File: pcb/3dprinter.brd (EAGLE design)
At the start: 100 x 80 mm, 24 parts, among them IC1 NRF51822, IC2 TMC2100

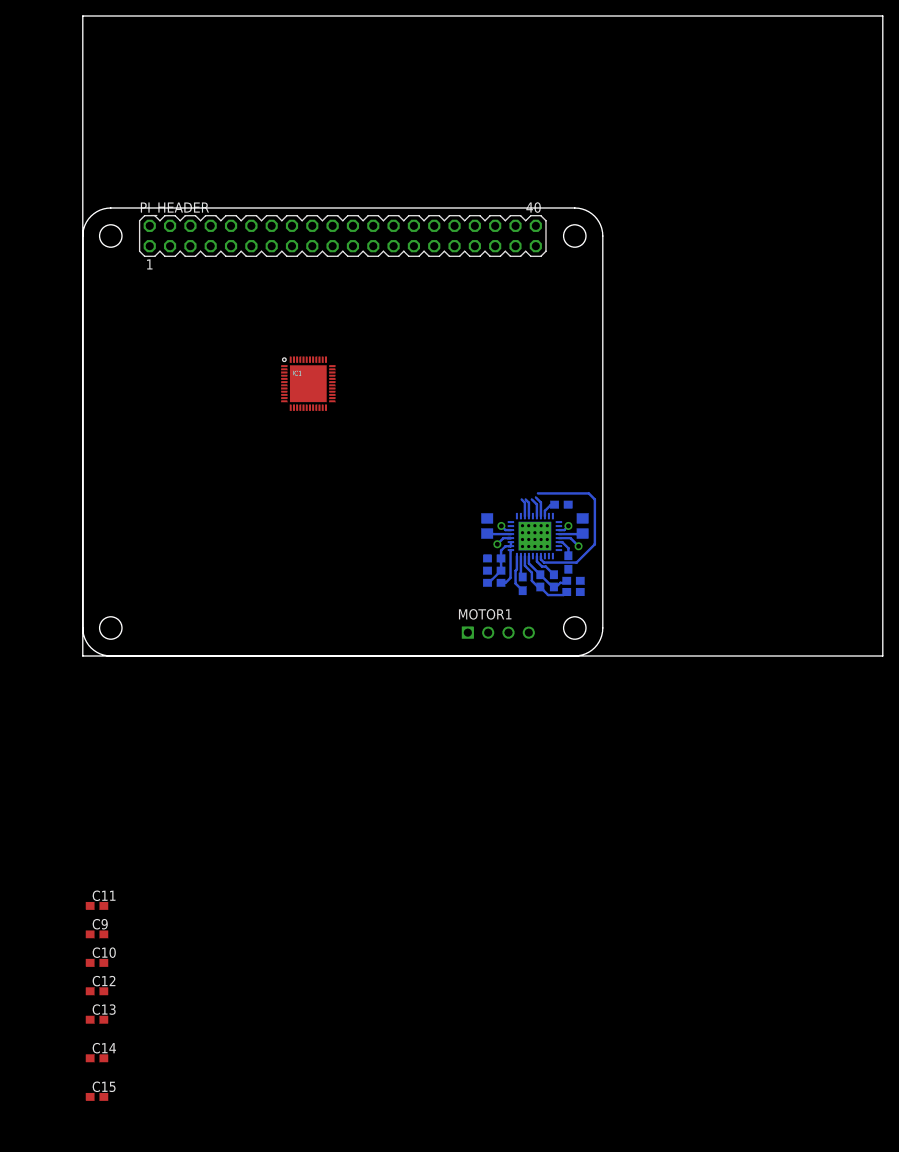
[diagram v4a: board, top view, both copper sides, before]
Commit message: Multiplied motor driver circuit and added mosfets
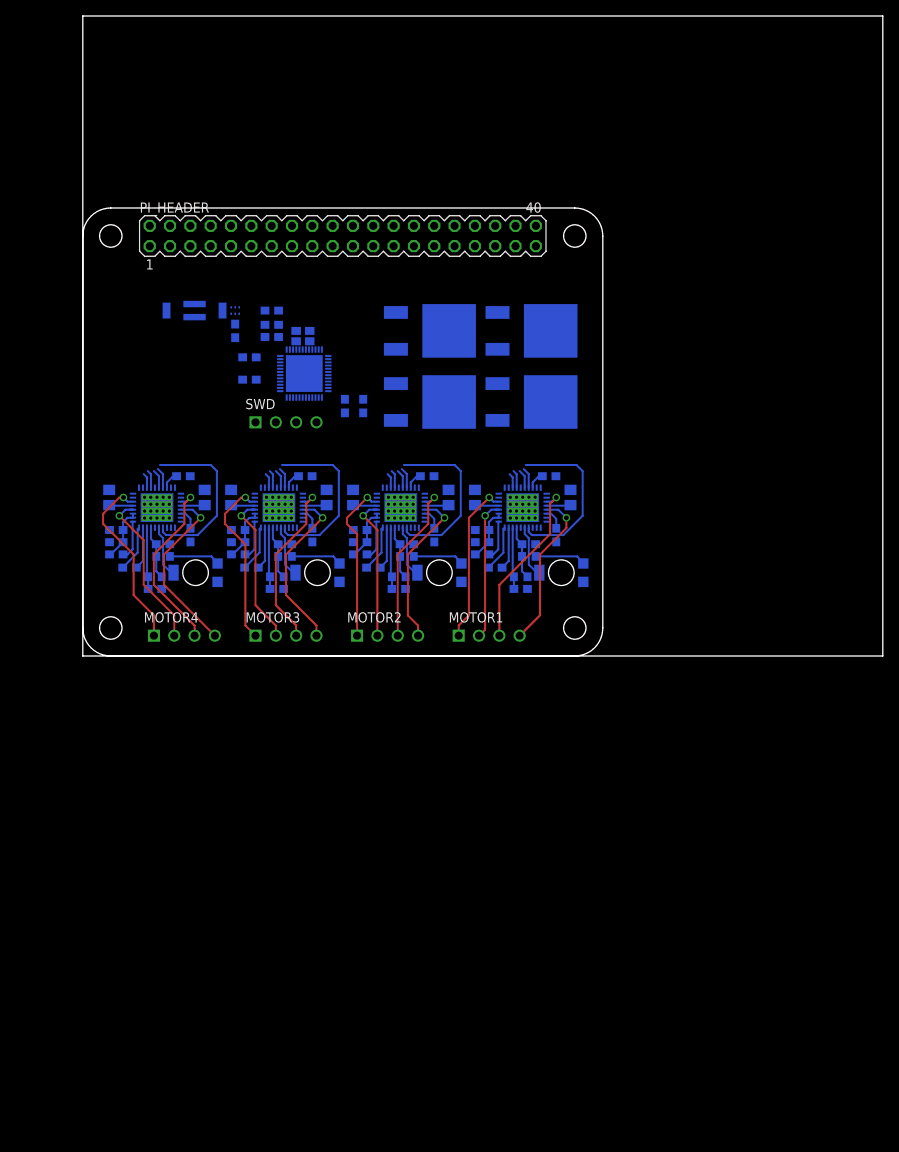
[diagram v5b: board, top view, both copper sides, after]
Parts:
- removed C2, C4, C5, C6: 100n, 3dprinter:C0603
- removed C3: 1u, 3dprinter:C0603
- removed C7: 470n, 3dprinter:C0603
- removed C8: 4.7u, 3dprinter:C0603
- removed IC2: TMC2100, 3dprinter:QFN36
- removed R1, R2: TBD, 3dprinter:R0805
- removed R3: TBD, 3dprinter:R0603
- removed R4: 2R2 / 3R3, 3dprinter:R0603
- added ANT: ANTENNA, 3dprinter:ANTENNA
- added BAL: BALUNBALUN, 3dprinter:BALUN
- added C1_M1, C1_M2, C1_M3, C1_M4, C2_M1, C2_M2, C2_M3, C2_M4, C4_M1, C4_M2, C4_M3, C4_M4, C5_M1, C5_M2, C5_M3, C5_M4, C6_M1, C6_M2, C6_M3, C6_M4: 100n, 3dprinter:C0603
- added C3_M1, C3_M2, C3_M3, C3_M4: 1u, 3dprinter:C0603
- added C7_M1, C7_M2, C7_M3, C7_M4: 470n, 3dprinter:C0603
- added C8_M1, C8_M2, C8_M3, C8_M4: 4.7u, 3dprinter:C0603
- added IC_M1, IC_M2, IC_M3, IC_M4: TMC2100, 3dprinter:QFN36
- added MOTOR2, MOTOR3, MOTOR4, SWD: (no value), 3dprinter:MA04-1
- added POT_M1, POT_M2, POT_M3, POT_M4: TRIMPOT, 3dprinter:TRIMPOT
- added Q1, Q2, Q3, Q4: MOSFET, 3dprinter:MOSFET
- added R1_M1, R1_M2, R1_M3, R1_M4: 20k, 3dprinter:R0603
- added R2_M1, R2_M2, R2_M3, R2_M4, R3_M1, R3_M2, R3_M3, R3_M4: TBD, 3dprinter:R0805
- added R4_M1, R4_M2, R4_M3, R4_M4: 2R2 / 3R3, 3dprinter:R0603
- added Y1: CRYSTAL, 3dprinter:CRYSTAL
- C1: value 100n -> 2.2n
- moved C15 94.4 mm to (20.8, 37.3), flipped to the bottom, turned to 180 degrees
- moved C14 88.1 mm to (35.1, 31.2), flipped to the bottom, turned to 270 degrees
- moved C12 87.8 mm to (23.6, 43.2), flipped to the bottom
- moved C13 82.7 mm to (32.8, 31.2), flipped to the bottom, turned to 270 degrees
- moved C9 79.3 mm to (23.6, 41.4), flipped to the bottom
- moved C10 75.3 mm to (20.8, 34.5), flipped to the bottom, turned to 180 degrees
- moved C11 74.4 mm to (23.6, 39.9), flipped to the bottom
- moved C1 44.1 mm to (19.1, 40.6), turned to 270 degrees
- moved IC1 1.37 mm to (27.7, 35.3), flipped to the bottom
- moved MOTOR1 1.20 mm to (50.8, 2.54)
- renumbered U$1 to OUTLINE
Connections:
- removed net IREF_M1: IC2.23, R3.1
- new net 5V_M2: C8_M2.1, IC_M2.25, R1_M2.2, R4_M2.2
- new net 5V_M3: C8_M3.1, IC_M3.25, R1_M3.2, R4_M3.2
- new net 5V_M4: C8_M4.1, IC_M4.25, R1_M4.2, R4_M4.2
- new net AIN_M1: IC_M1.23, POT_M1.2
- new net AIN_M2: IC_M2.23, POT_M2.2
- new net AIN_M3: IC_M3.23, POT_M3.2
- new net AIN_M4: IC_M4.23, POT_M4.2
- new net BRA_M2: IC_M2.33, R3_M2.2
- new net BRA_M3: IC_M3.33, R3_M3.2
- new net BRA_M4: IC_M4.33, R3_M4.2
- new net BRB_M2: IC_M2.14, R2_M2.2
- new net BRB_M3: IC_M3.14, R2_M3.2
- new net BRB_M4: IC_M4.14, R2_M4.2
- new net CFG1_M2: IC_M2.4
- new net CFG1_M3: IC_M3.4
- new net CFG1_M4: IC_M4.4
- new net CFG2_M2: IC_M2.3
- new net CFG2_M3: IC_M3.3
- new net CFG2_M4: IC_M4.3
- new net CPI_M2: C5_M2.1, IC_M2.28
- new net CPI_M3: C5_M3.1, IC_M3.28
- new net CPI_M4: C5_M4.1, IC_M4.28
- new net CPO_M2: C5_M2.2, IC_M2.27
- new net CPO_M3: C5_M3.2, IC_M3.27
- new net CPO_M4: C5_M4.2, IC_M4.27
- new net DIR_M2: IC_M2.7
- new net DIR_M3: IC_M3.7
- new net DIR_M4: IC_M4.7
- new net EN_M2: IC_M2.22
- new net EN_M3: IC_M3.22
- new net EN_M4: IC_M4.22
- new net N$10: BAL.4, IC1.32
- new net N$7: ANT.1, BAL.1
- new net N$8: BAL.5, C1.1, IC1.30
- new net N$9: BAL.3, IC1.31
- new net OA1_M2: IC_M2.34, MOTOR2.1
- new net OA1_M3: IC_M3.34, MOTOR3.1
- new net OA1_M4: IC_M4.34, MOTOR4.1
- new net OA2_M2: IC_M2.32, MOTOR2.2
- new net OA2_M3: IC_M3.32, MOTOR3.2
- new net OA2_M4: IC_M4.32, MOTOR4.2
- new net OB1_M2: IC_M2.13, MOTOR2.3
- new net OB1_M3: IC_M3.13, MOTOR3.3
- new net OB1_M4: IC_M4.13, MOTOR4.3
- new net OB2_M2: IC_M2.15, MOTOR2.4
- new net OB2_M3: IC_M3.15, MOTOR3.4
- new net OB2_M4: IC_M4.15, MOTOR4.4
- new net POT_M1: POT_M1.1, R1_M1.1
- new net POT_M2: POT_M2.1, R1_M2.1
- new net POT_M3: POT_M3.1, R1_M3.1
- new net POT_M4: POT_M4.1, R1_M4.1
- new net STEP_M2: IC_M2.6
- new net STEP_M3: IC_M3.6
- new net STEP_M4: IC_M4.6
- new net SWDCLK: IC1.24, SWD.2
- new net SWDIO: IC1.23, SWD.3
- new net VCC_M2: C7_M2.1, IC_M2.26, R4_M2.1
- new net VCC_M3: C7_M3.1, IC_M3.26, R4_M3.1
- new net VCC_M4: C7_M4.1, IC_M4.26, R4_M4.1
- new net VCP_M2: C4_M2.1, IC_M2.29
- new net VCP_M3: C4_M3.1, IC_M3.29
- new net VCP_M4: C4_M4.1, IC_M4.29
- net +12V: now also C1_M1.2, C1_M2.2, C1_M3.2, C1_M4.2, C2_M1.2, C2_M2.2, C2_M3.2, C2_M4.2, C3_M1.2, C3_M2.2, C3_M3.2, C3_M4.2, C4_M1.2, C4_M2.2, C4_M3.2, C4_M4.2, IC_M1.16, IC_M1.30, IC_M1.31, IC_M2.16, IC_M2.30, IC_M2.31, IC_M3.16, IC_M3.30, IC_M3.31, IC_M4.16, IC_M4.30, IC_M4.31; no longer C1.2, C2.2, C3.2, C4.2, IC2.16, IC2.30, IC2.31
- net +3V3: now also C13.1, C14.1, IC1.1, IC1.12; no longer PI_HEADER.1, PI_HEADER.17
- net +5V: now also C6_M1.1, C6_M2.1, C6_M3.1, C6_M4.1, IC_M1.8, IC_M2.8, IC_M3.8, IC_M4.8; no longer C6.1, IC2.8
- net 5V_M1: now also C8_M1.1, IC_M1.25, R1_M1.2, R4_M1.2; no longer C8.1, IC2.25, R3.2, R4.2
- net BRA_M1: now also IC_M1.33, R3_M1.2; no longer IC2.33, R2.2
- net BRB_M1: now also IC_M1.14, R2_M1.2; no longer IC2.14, R1.2
- net CFG1_M1: now also IC_M1.4; no longer IC2.4
- net CFG2_M1: now also IC_M1.3; no longer IC2.3
- net CPI_M1: now also C5_M1.1, IC_M1.28; no longer C5.1, IC2.28
- net CPO_M1: now also C5_M1.2, IC_M1.27; no longer C5.2, IC2.27
- net DIR_M1: now also IC_M1.7; no longer IC2.7
- net EN_M1: now also IC_M1.22; no longer IC2.22
- net GND: now also BAL.2, BAL.6, C1.2, C1_M1.1, C1_M2.1, C1_M3.1, C1_M4.1, C2_M1.1, C2_M2.1, C2_M3.1, C2_M4.1, C3_M1.1, C3_M2.1, C3_M3.1, C3_M4.1, C6_M1.2, C6_M2.2, C6_M3.2, C6_M4.2, C7_M1.2, C7_M2.2, C7_M3.2, C7_M4.2, C8_M1.2, C8_M2.2, C8_M3.2, C8_M4.2, IC_M1.1, IC_M1.10, IC_M1.11, IC_M1.12, IC_M1.24, IC_M1.35, IC_M1.36, IC_M1.5, IC_M1.PAD, IC_M1.TVIA1, IC_M1.TVIA10, IC_M1.TVIA11, IC_M1.TVIA12, IC_M1.TVIA13, IC_M1.TVIA14, IC_M1.TVIA15, IC_M1.TVIA16, IC_M1.TVIA17, IC_M1.TVIA18, IC_M1.TVIA19, IC_M1.TVIA2, IC_M1.TVIA20, IC_M1.TVIA3, IC_M1.TVIA4, IC_M1.TVIA5, IC_M1.TVIA6, IC_M1.TVIA7, IC_M1.TVIA8, IC_M1.TVIA9, IC_M2.1, IC_M2.10, IC_M2.11, IC_M2.12, IC_M2.24, IC_M2.35, IC_M2.36, IC_M2.5, IC_M2.PAD, IC_M2.TVIA1, IC_M2.TVIA10, IC_M2.TVIA11, IC_M2.TVIA12, IC_M2.TVIA13, IC_M2.TVIA14, IC_M2.TVIA15, IC_M2.TVIA16, IC_M2.TVIA17, IC_M2.TVIA18, IC_M2.TVIA19, IC_M2.TVIA2, IC_M2.TVIA20, IC_M2.TVIA3, IC_M2.TVIA4, IC_M2.TVIA5, IC_M2.TVIA6, IC_M2.TVIA7, IC_M2.TVIA8, IC_M2.TVIA9, IC_M3.1, IC_M3.10, IC_M3.11, IC_M3.12, IC_M3.24, IC_M3.35, IC_M3.36, IC_M3.5, IC_M3.PAD, IC_M3.TVIA1, IC_M3.TVIA10, IC_M3.TVIA11, IC_M3.TVIA12, IC_M3.TVIA13, IC_M3.TVIA14, IC_M3.TVIA15, IC_M3.TVIA16, IC_M3.TVIA17, IC_M3.TVIA18, IC_M3.TVIA19, IC_M3.TVIA2, IC_M3.TVIA20, IC_M3.TVIA3, IC_M3.TVIA4, IC_M3.TVIA5, IC_M3.TVIA6, IC_M3.TVIA7, IC_M3.TVIA8, IC_M3.TVIA9, IC_M4.1, IC_M4.10, IC_M4.11, IC_M4.12, IC_M4.24, IC_M4.35, IC_M4.36, IC_M4.5, IC_M4.PAD, IC_M4.TVIA1, IC_M4.TVIA10, IC_M4.TVIA11, IC_M4.TVIA12, IC_M4.TVIA13, IC_M4.TVIA14, IC_M4.TVIA15, IC_M4.TVIA16, IC_M4.TVIA17, IC_M4.TVIA18, IC_M4.TVIA19, IC_M4.TVIA2, IC_M4.TVIA20, IC_M4.TVIA3, IC_M4.TVIA4, IC_M4.TVIA5, IC_M4.TVIA6, IC_M4.TVIA7, IC_M4.TVIA8, IC_M4.TVIA9, POT_M1.3, POT_M2.3, POT_M3.3, POT_M4.3, R2_M1.1, R2_M2.1, R2_M3.1, R2_M4.1, R3_M1.1, R3_M2.1, R3_M3.1, R3_M4.1, SWD.1, Y1.2, Y1.4; no longer C1.1, C2.1, C3.1, C6.2, C7.2, C8.2, IC2.1, IC2.10, IC2.11, IC2.12, IC2.24, IC2.35, IC2.36, IC2.5, IC2.PAD, IC2.TVIA1, IC2.TVIA10, IC2.TVIA11, IC2.TVIA12, IC2.TVIA13, IC2.TVIA14, IC2.TVIA15, IC2.TVIA16, IC2.TVIA17, IC2.TVIA18, IC2.TVIA19, IC2.TVIA2, IC2.TVIA20, IC2.TVIA3, IC2.TVIA4, IC2.TVIA5, IC2.TVIA6, IC2.TVIA7, IC2.TVIA8, IC2.TVIA9, R1.1, R2.1
- net N$1: now also Y1.1
- net N$2: now also Y1.3
- net N$5: now also PI_HEADER.1, PI_HEADER.17; no longer C13.1, C14.1, IC1.1, IC1.12
- net OA1_M1: now also IC_M1.34; no longer IC2.34
- net OA2_M1: now also IC_M1.32; no longer IC2.32
- net OB1_M1: now also IC_M1.13; no longer IC2.13
- net OB2_M1: now also IC_M1.15; no longer IC2.15
- net STEP_M1: now also IC_M1.6; no longer IC2.6
- net VCC_M1: now also C7_M1.1, IC_M1.26, R4_M1.1; no longer C7.1, IC2.26, R4.1
- net VCP_M1: now also C4_M1.1, IC_M1.29; no longer C4.1, IC2.29
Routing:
- net +12V: track 9.24 -> 37.8 mm
- net OB1_M4: track 0.00 -> 22.7 mm, vias 0 -> 1
- net OA1_M4: track 0.00 -> 22.7 mm, vias 0 -> 1
- net OB2_M4: track 0.00 -> 22.1 mm, vias 0 -> 1
- net OB1_M3: track 0.00 -> 21.6 mm, vias 0 -> 1
- net OA1_M3: track 0.00 -> 21.6 mm, vias 0 -> 1
- net EN_M4: track 0.00 -> 21.5 mm
- net EN_M3: track 0.00 -> 21.5 mm
- net EN_M2: track 0.00 -> 21.5 mm
- net OB2_M3: track 0.00 -> 21.1 mm, vias 0 -> 1
- net OB1_M2: track 0.00 -> 20.6 mm, vias 0 -> 1
- net OA2_M4: track 0.00 -> 20.3 mm, vias 0 -> 1
- net OA1_M2: track 0.00 -> 20.3 mm, vias 0 -> 1
- net OB1_M1: track 1.41 -> 21.6 mm
- net OB2_M2: track 0.00 -> 20.0 mm, vias 0 -> 1
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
